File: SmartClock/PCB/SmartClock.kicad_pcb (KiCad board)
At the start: 2 copper layers, 53 x 30 mm, 4 parts, among them SW1 SW_Push, U2 XIAO-ESP32-C3-DIP

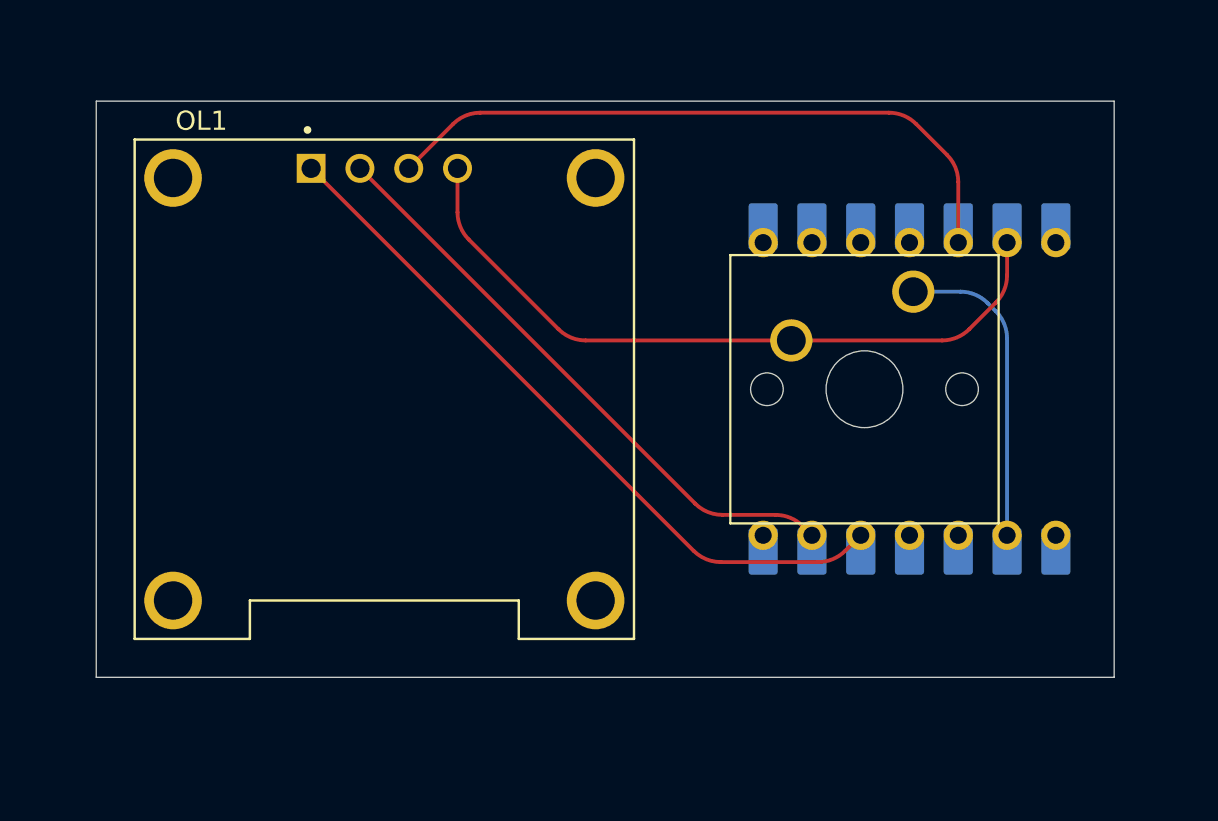
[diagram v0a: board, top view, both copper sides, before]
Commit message: added GND planes and fillets
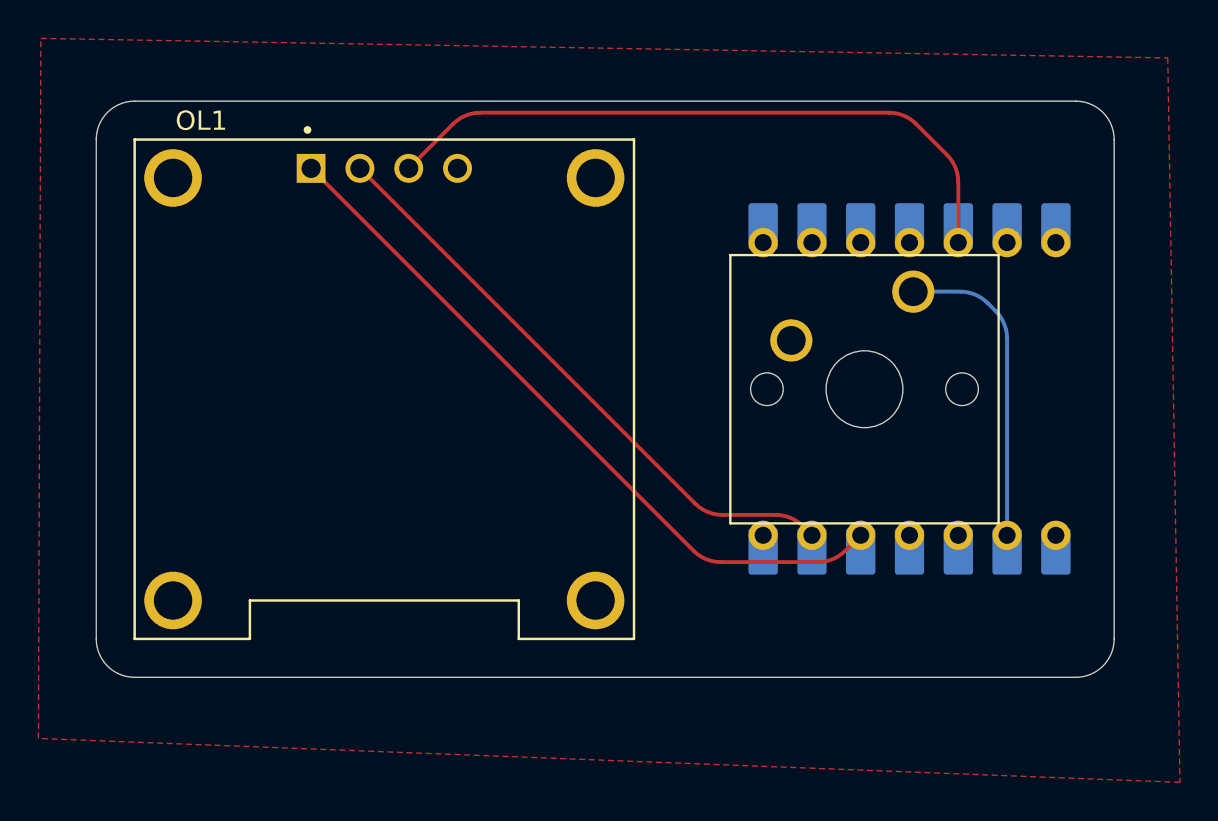
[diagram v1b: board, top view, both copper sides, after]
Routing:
- net GND: track 37.4 -> 0.00 mm
- added copper zone on F.Cu, net GND
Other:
- outline, holes or cut-outs redrawn
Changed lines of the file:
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@@
 		)
 	)
-	(gr_rect
-		(start 105.5 34)
-		(end 158.5 64)
-		(stroke
-			(width 0.05)
-			(type default)
-		)
-		(fill no)
+	(gr_arc
+		(start 158.5 62)
+		(mid 157.914214 63.414214)
+		(end 156.5 64)
+		(stroke
+			(width 0.05)
+			(type default)
+		)
+		(layer "Edge.Cuts")
+	)
+	(gr_arc
+		(start 156.5 34)
+		(mid 157.914214 34.585786)
+		(end 158.5 36)
+		(stroke
+			(width 0.05)
+			(type default)
+		)
+		(layer "Edge.Cuts")
+	)
+	(gr_line
+		(start 158.5 36)
+		(end 158.5 62)
+		(stroke
+			(width 0.05)
+			(type default)
+		)
+		(layer "Edge.Cuts")
+	)
+	(gr_arc
+		(start 107.5 64)
+		(mid 106.085786 63.414214)
+		(end 105.5 62)
+		(stroke
+			(width 0.05)
+			(type default)
+		)
+		(layer "Edge.Cuts")
+	)
+	(gr_line
+		(start 105.5 62)
+		(end 105.5 36)
+		(stroke
+			(width 0.05)
+			(type default)
+		)
+		(layer "Edge.Cuts")
+	)
+	(gr_arc
+		(start 105.5 36)
+		(mid 106.085786 34.585786)
+		(end 107.5 34)
+		(stroke
+			(width 0.05)
+			(type default)
+		)
+		(layer "Edge.Cuts")
+	)
+	(gr_line
+		(start 107.5 34)
+		(end 156.5 34)
+		(stroke
+			(width 0.05)
+			(type default)
+		)
+		(layer "Edge.Cuts")
+	)
+	(gr_line
+		(start 156.5 64)
+		(end 107.5 64)
+		(stroke
+			(width 0.05)
+			(type default)
+		)
 		(layer "Edge.Cuts")
 	)
@@
 		(net 4)
 	)
-	(segment
-		(start 141.69 46.46)
-		(end 149.541296 46.46)
-		(width 0.2)
-		(layer "F.Cu")
+	(zone
 		(net 13)
-	)
-	(segment
-		(start 152.923962 43.077334)
-		(end 152.923962 41.365761)
-		(width 0.2)
-		(layer "F.Cu")
-		(net 13)
-	)
-	(segment
-		(start 130.981427 46.46)
-		(end 141.69 46.46)
-		(width 0.2)
-		(layer "F.Cu")
-		(net 13)
-	)
-	(segment
-		(start 124.31 37.5)
-		(end 124.31 39.788573)
-		(width 0.2)
-		(layer "F.Cu")
-		(net 13)
-	)
-	(segment
-		(start 150.95551 45.874213)
-		(end 152.338176 44.491547)
-		(width 0.2)
-		(layer "F.Cu")
-		(net 13)
-	)
-	(segment
-		(start 124.895787 41.202787)
-		(end 129.567214 45.874214)
-		(width 0.2)
-		(layer "F.Cu")
-		(net 13)
-	)
-	(arc
-		(start 124.31 39.788573)
-		(mid 124.462241 40.55394)
-		(end 124.895787 41.202787)
-		(width 0.2)
-		(layer "F.Cu")
-		(net 13)
-	)
-	(arc
-		(start 152.923962 43.077334)
-		(mid 152.771721 43.842701)
-		(end 152.338176 44.491547)
-		(width 0.2)
-		(layer "F.Cu")
-		(net 13)
-	)
-	(arc
-		(start 149.541296 46.46)
-		(mid 150.306663 46.307759)
-		(end 150.95551 45.874213)
-		(width 0.2)
-		(layer "F.Cu")
-		(net 13)
-	)
-	(arc
-		(start 130.981427 46.46)
-		(mid 130.21606 46.307759)
-		(end 129.567214 45.874214)
-		(width 0.2)
-		(layer "F.Cu")
-		(net 13)
+		(net_name "GND")
+		(layer "F.Cu")
+		(hatch edge 0.5)
+		(connect_pads
+			(clearance 0.5)
+		)
+		(min_thickness 0.25)
+		(filled_areas_thickness no)
+		(fill yes
+			(thermal_gap 0.5)
+			(thermal_bridge_width 0.5)
+		)
+		(polygon
+			(pts
+				(xy 102.616 30.734) (xy 161.29 31.75) (xy 161.925 69.469) (xy 102.489 67.183) (xy 102.616 30.734)
+			)
+		)
 	)
 	(embedded_fonts no)

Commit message: fixed pins
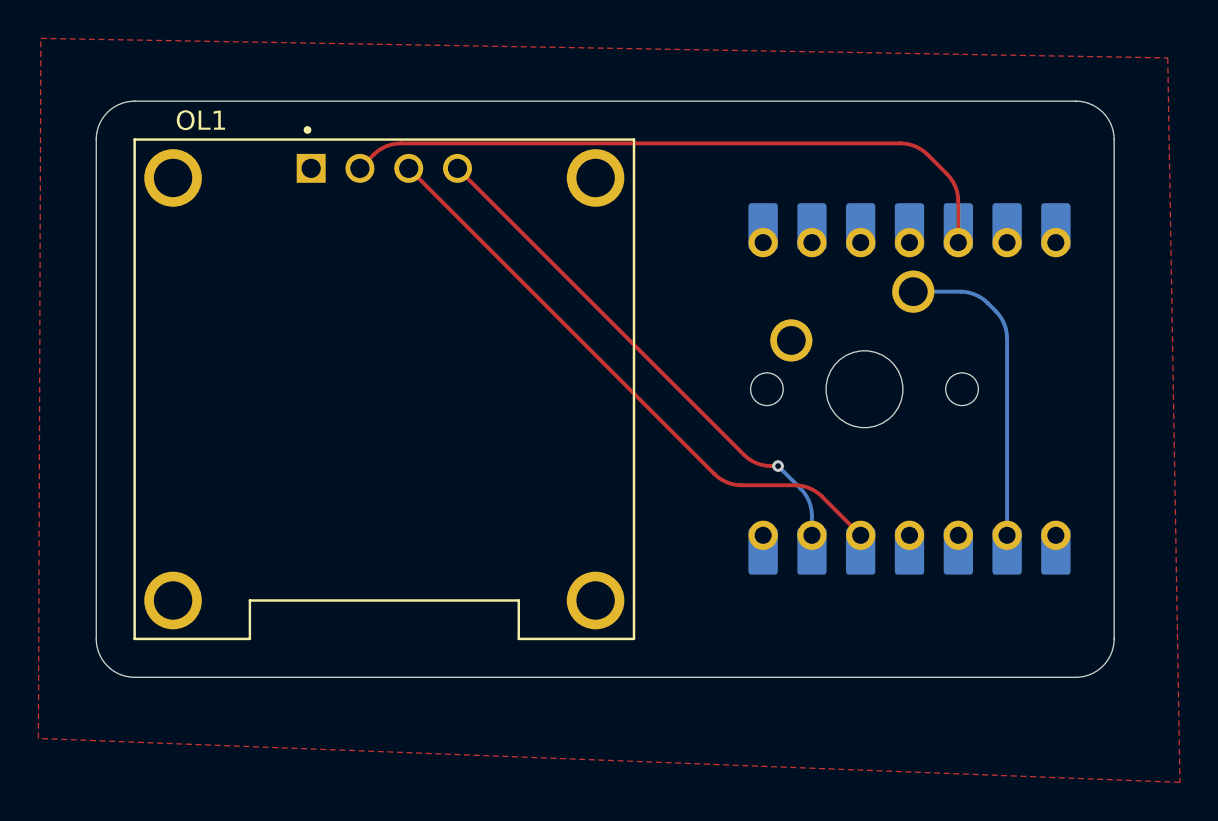
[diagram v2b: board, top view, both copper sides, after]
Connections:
- OL1 pad 1: Net-(OL1-SDA) -> GND
- OL1 pad 2: Net-(OL1-SCL) -> Net-(OL1-VCC)
- OL1 pad 3: Net-(OL1-VCC) -> Net-(OL1-SCL)
- OL1 pad 4: GND -> Net-(OL1-SDA)
- U2 pad 5: Net-(OL1-SDA) -> Net-(OL1-SCL)
- U2 pad 6: Net-(OL1-SCL) -> Net-(OL1-SDA)
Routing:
- net Net-(OL1-SDA): track 37.5 -> 27.9 mm, vias 0 -> 1
- net Net-(OL1-VCC): track 34.7 -> 35.3 mm
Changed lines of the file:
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@@
 			(drillshape 0)
 			(scaleselection 1)
-			(outputdirectory "./")
+			(outputdirectory "Gerber/")
 		)
 	)
@@
 			(layers "*.Cu" "*.Mask")
 			(remove_unused_layers no)
-			(net 3 "Net-(OL1-SDA)")
-			(pinfunction "SDA")
-			(pintype "bidirectional")
+			(net 13 "GND")
+			(pinfunction "GND")
+			(pintype "power_in")
 			(solder_mask_margin 0.102)
 		)
@@
 			(layers "*.Cu" "*.Mask")
 			(remove_unused_layers no)
-			(net 1 "Net-(OL1-SCL)")
-			(pinfunction "SCL")
-			(pintype "bidirectional")
+			(net 2 "Net-(OL1-VCC)")
+			(pinfunction "VCC")
+			(pintype "power_in")
 			(solder_mask_margin 0.102)
 		)
@@
 			(layers "*.Cu" "*.Mask")
 			(remove_unused_layers no)
-			(net 2 "Net-(OL1-VCC)")
-			(pinfunction "VCC")
-			(pintype "power_in")
+			(net 1 "Net-(OL1-SCL)")
+			(pinfunction "SCL")
+			(pintype "input")
 			(solder_mask_margin 0.102)
 		)
@@
 			(layers "*.Cu" "*.Mask")
 			(remove_unused_layers no)
-			(net 13 "GND")
-			(pinfunction "GND")
-			(pintype "power_in")
+			(net 3 "Net-(OL1-SDA)")
+			(pinfunction "SDA")
+			(pintype "bidirectional")
 			(solder_mask_margin 0.102)
 		)
@@
 		)
 		(embedded_fonts no)
-		(model "H:/Downloads/DM-OLED096-636/DM-OLED096-636.step"
-			(offset
-				(xyz 0 0 0)
-			)
-			(scale
-				(xyz 1 1 1)
-			)
-			(rotate
-				(xyz -90 -0 -0)
-			)
-		)
 	)
 	(footprint "Button_Switch_Keyboard:SW_Cherry_MX_1.00u_PCB"
@@
 		(attr through_hole)
 		(fp_line
-			(start -9.525 -1.905)
-			(end 4.445 -1.905)
-			(stroke
-				(width 0.12)
-				(type solid)
-			)
-			(layer "F.SilkS")
-		)
-		(fp_line
-			(start -9.525 12.065)
-			(end -9.525 -1.905)
-			(stroke
-				(width 0.12)
-				(type solid)
-			)
-			(layer "F.SilkS")
-		)
-		(fp_line
-			(start 4.445 -1.905)
-			(end 4.445 12.065)
-			(stroke
-				(width 0.12)
-				(type solid)
-			)
-			(layer "F.SilkS")
-		)
-		(fp_line
-			(start 4.445 12.065)
-			(end -9.525 12.065)
-			(stroke
-				(width 0.12)
-				(type solid)
-			)
-			(layer "F.SilkS")
-		)
-		(fp_line
-			(start -12.065 -4.445)
-			(end 6.985 -4.445)
-			(stroke
-				(width 0.15)
-				(type solid)
-			)
-			(layer "Dwgs.User")
-		)
-		(fp_line
-			(start -12.065 14.605)
-			(end -12.065 -4.445)
-			(stroke
-				(width 0.15)
-				(type solid)
-			)
-			(layer "Dwgs.User")
-		)
-		(fp_line
-			(start 6.985 -4.445)
-			(end 6.985 14.605)
-			(stroke
-				(width 0.15)
-				(type solid)
-			)
-			(layer "Dwgs.User")
-		)
-		(fp_line
-			(start 6.985 14.605)
-			(end -12.065 14.605)
-			(stroke
-				(width 0.15)
-				(type solid)
-			)
-			(layer "Dwgs.User")
-		)
-		(fp_line
 			(start -9.14 -1.52)
 			(end 4.06 -1.52)
@@
 			(layers "*.Cu" "*.Mask")
 			(remove_unused_layers no)
-			(net 3 "Net-(OL1-SDA)")
+			(net 1 "Net-(OL1-SCL)")
 			(pinfunction "GPIO6_D4_SDA")
 			(pintype "passive")
@@
 			(layers "B.Cu" "B.Mask")
 			(roundrect_rratio 0.1)
-			(net 3 "Net-(OL1-SDA)")
+			(net 1 "Net-(OL1-SCL)")
 			(pinfunction "GPIO6_D4_SDA")
 			(pintype "passive")
@@
 			(layers "*.Cu" "*.Mask")
 			(remove_unused_layers no)
-			(net 1 "Net-(OL1-SCL)")
+			(net 3 "Net-(OL1-SDA)")
 			(pinfunction "GPIO7_D5_SCL")
 			(pintype "passive")
@@
 			(layers "B.Cu" "B.Mask")
 			(roundrect_rratio 0.1)
-			(net 1 "Net-(OL1-SCL)")
+			(net 3 "Net-(OL1-SDA)")
 			(pinfunction "GPIO7_D5_SCL")
 			(pintype "passive")
@@
 	)
 	(segment
-		(start 119.23 37.5)
-		(end 136.686975 54.956975)
+		(start 145.303962 56.605761)
+		(end 144.954862 56.954861)
 		(width 0.2)
 		(layer "F.Cu")
@@
 	)
 	(segment
-		(start 142.286749 56.128548)
-		(end 142.763962 56.605761)
+		(start 143.283988 54.585787)
+		(end 145.303962 56.605761)
+		(width 0.2)
+		(layer "F.Cu")
+		(net 1)
+	)
+	(segment
+		(start 139.098427 54)
+		(end 141.869774 54)
 		(width 0.2)
 		(layer "F.Cu")
@@
 	)
 	(segment
-		(start 138.101188 55.542761)
-		(end 140.872535 55.542761)
+		(start 121.77 37.5)
+		(end 137.684214 53.414214)
+		(width 0.2)
+		(layer "F.Cu")
+		(net 1)
+	)
+	(segment
+		(start 144.954862 56.954861)
+		(end 144.954861 56.954861)
 		(width 0.2)
 		(layer "F.Cu")
@@
 	)
 	(arc
-		(start 140.872535 55.542761)
-		(mid 141.637902 55.695002)
-		(end 142.286749 56.128548)
+		(start 137.684214 53.414214)
+		(mid 138.33306 53.847759)
+		(end 139.098427 54)
 		(width 0.2)
 		(layer "F.Cu")
@@
 	)
 	(arc
-		(start 138.101188 55.542761)
-		(mid 137.335821 55.39052)
-		(end 136.686975 54.956975)
+		(start 143.283988 54.585787)
+		(mid 142.635141 54.152241)
+		(end 141.869774 54)
 		(width 0.2)
 		(layer "F.Cu")
@@
 	)
 	(segment
-		(start 125.497427 34.601)
-		(end 146.772573 34.601)
+		(start 119.23 37.5)
+		(end 119.945214 36.784786)
 		(width 0.2)
 		(layer "F.Cu")
@@
 	)
 	(segment
-		(start 150.383962 38.212389)
-		(end 150.383962 41.365761)
+		(start 148.784787 36.784787)
+		(end 149.798176 37.798176)
 		(width 0.2)
 		(layer "F.Cu")
@@
 	)
 	(segment
-		(start 121.77 37.5)
-		(end 124.083214 35.186786)
+		(start 150.383962 39.212389)
+		(end 150.383962 41.365761)
 		(width 0.2)
 		(layer "F.Cu")
@@
 	)
 	(segment
-		(start 148.186787 35.186787)
-		(end 149.798176 36.798176)
+		(start 121.359427 36.199)
+		(end 147.370573 36.199)
 		(width 0.2)
 		(layer "F.Cu")
@@
 	)
 	(arc
-		(start 146.772573 34.601)
-		(mid 147.53794 34.753241)
-		(end 148.186787 35.186787)
+		(start 119.945214 36.784786)
+		(mid 120.59406 36.351241)
+		(end 121.359427 36.199)
 		(width 0.2)
 		(layer "F.Cu")
@@
 	)
 	(arc
-		(start 125.497427 34.601)
-		(mid 124.73206 34.753241)
-		(end 124.083214 35.186786)
+		(start 148.784787 36.784787)
+		(mid 148.13594 36.351241)
+		(end 147.370573 36.199)
 		(width 0.2)
 		(layer "F.Cu")
@@
 	)
 	(arc
-		(start 150.383962 38.212389)
-		(mid 150.231721 37.447022)
-		(end 149.798176 36.798176)
+		(start 149.798176 37.798176)
+		(mid 150.231721 38.447022)
+		(end 150.383962 39.212389)
 		(width 0.2)
 		(layer "F.Cu")
@@
 	)
 	(segment
-		(start 144.495509 57.414213)
-		(end 144.954861 56.954861)
+		(start 124.31 37.5)
+		(end 139.224214 52.414214)
 		(width 0.2)
 		(layer "F.Cu")
@@
 	)
 	(segment
-		(start 145.303962 56.605761)
-		(end 144.954862 56.954861)
+		(start 140.638427 53)
+		(end 141 53)
 		(width 0.2)
 		(layer "F.Cu")
@@
 	)
 	(segment
-		(start 138.018427 58)
-		(end 143.081295 58)
+		(start 142.286749 56.128548)
+		(end 142.763962 56.605761)
 		(width 0.2)
 		(layer "F.Cu")
 		(net 3)
 	)
-	(segment
-		(start 144.954862 56.954861)
-		(end 144.954861 56.954861)
+	(via
+		(at 141 53)
+		(size 0.6)
+		(drill 0.3)
+		(layers "F.Cu" "B.Cu")
+		(net 3)
+	)
+	(arc
+		(start 139.224214 52.414214)
+		(mid 139.87306 52.847759)
+		(end 140.638427 53)
 		(width 0.2)
 		(layer "F.Cu")
@@
 	)
 	(segment
-		(start 116.69 37.5)
-		(end 136.604214 57.414214)
+		(start 142.763962 55.592389)
+		(end 142.763962 56.605761)
 		(width 0.2)
-		(layer "F.Cu")
+		(layer "B.Cu")
 		(net 3)
 	)
-	(arc
-		(start 136.604214 57.414214)
-		(mid 137.25306 57.847759)
-		(end 138.018427 58)
+	(segment
+		(start 141 53)
+		(end 142.178176 54.178176)
 		(width 0.2)
-		(layer "F.Cu")
+		(layer "B.Cu")
 		(net 3)
 	)
 	(arc
-		(start 143.081295 58)
-		(mid 143.846662 57.847759)
-		(end 144.495509 57.414213)
+		(start 142.763962 55.592389)
+		(mid 142.611721 54.827022)
+		(end 142.178176 54.178176)
 		(width 0.2)
-		(layer "F.Cu")
+		(layer "B.Cu")
 		(net 3)
 	)
@@
 		(polygon
 			(pts
-				(xy 102.616 30.734) (xy 161.29 31.75) (xy 161.925 69.469) (xy 102.489 67.183) (xy 102.616 30.734)
+				(xy 102.616 30.734) (xy 161.29 31.75) (xy 161.925 69.469) (xy 102.489 67.183)
 			)
 		)
